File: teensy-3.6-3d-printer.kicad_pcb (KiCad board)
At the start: 2 copper layers, 128.3 x 100.3 mm, 89 parts, among them J1 X_STEPPER, J10 AUX_STEPPER, J11 X-Min-Limit, J12 X-Max-Limit, J13 Y-Min-Limit, J14 Y-Max-Limit, J15 Z-Min-Limit, J16 Z-Max-Limit, J17 Temp0, J18 Temp1, J19 Bed-Temp, J2 Y_STEPPER, J20 3.3V, J21 5V, J22 Conn_02x20_Counter_Clockwise, J23 GND, J25 teensy_back_pins, J26 Extruder 0 Fan, J27 Extruder 0 Part Fan, J28 Aux Fan, J29 12V, J3 Z_STEPPER, J30 12V, J31 Debug, J32 Printer Power IN, J33 Heated Bed, J34 Hot End 1, J35 Hot End 0, J36 12V, J37 Aux 2 Fan, J4 E0_STEPPER, J5 AUX_STEPPER, J6 X_STEPPER, J7 Y_STEPPER, J8 Z_STEPPER, J9 E0_STEPPER, Q1 PN2222A, Q2 PN2222A, Q3 PN2222A, Q4 PN2222A, Q5 IRLZ44N, Q6 PN2222A, Q7 IRLZ44N, U1 Zonestar-LCD2004, U2 Teensy3.6, U3 L7805

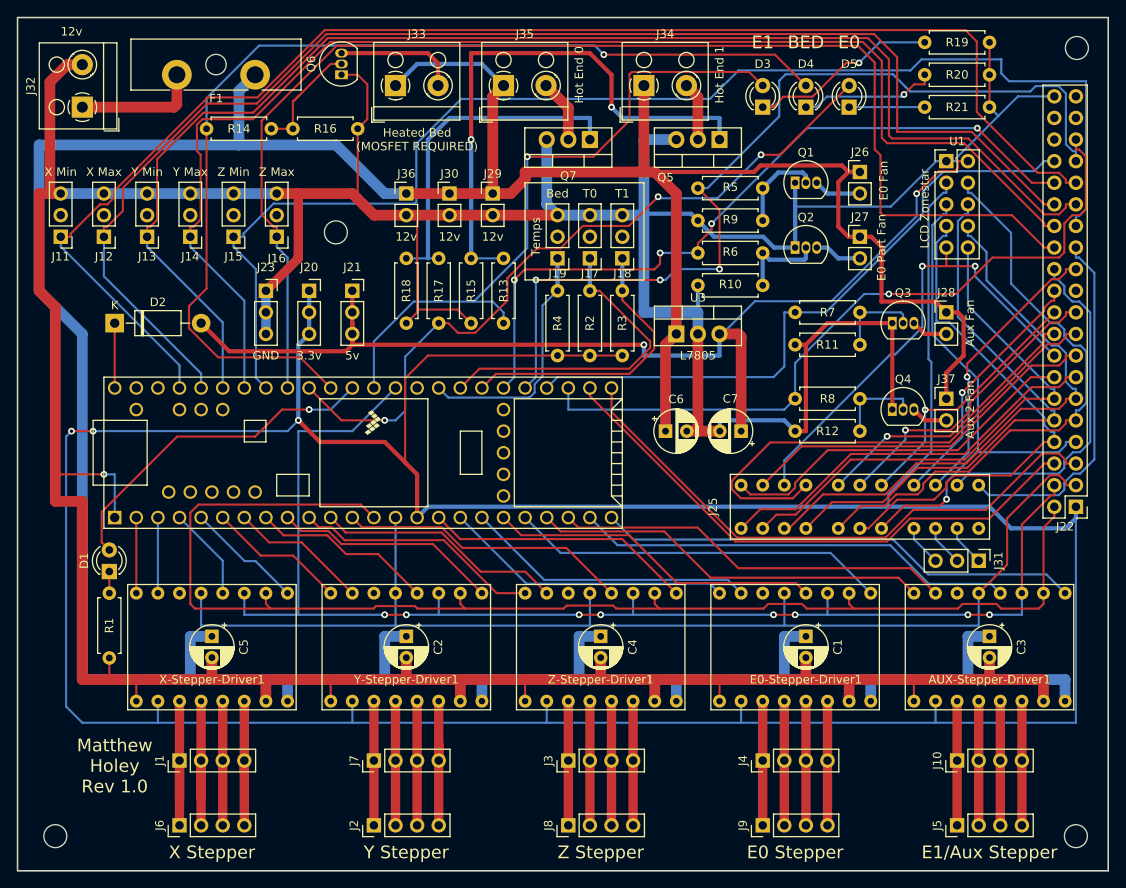
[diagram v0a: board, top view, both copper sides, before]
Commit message: Changed to new fuse holder, added filled zones
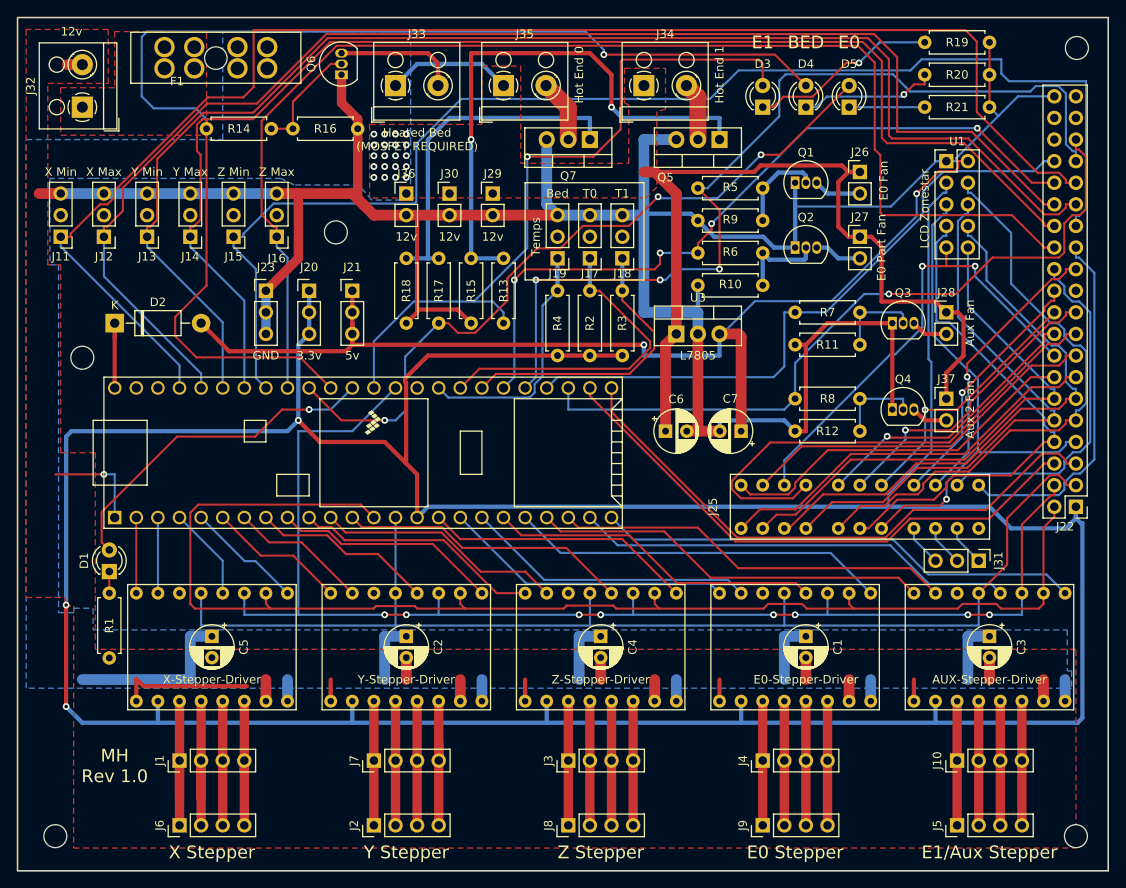
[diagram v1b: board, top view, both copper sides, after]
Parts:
- added REF**: MountingHole_2.7mm_M2.5, MountingHole:MountingHole_2.7mm_M2.5, F.Cu at (101.6, 56.1)
- F1: footprint Fuse:Fuseholder_Blade_ATO_Littelfuse_Pudenz_2_Pin -> fuse:Pudenz-30a-PCB-ATO-Fuseholder
- J20, J21, J23: footprint Connector_PinSocket_2.54mm:PinSocket_1x03_P2.54mm_Vertical -> Connector_PinHeader_2.54mm:PinHeader_1x03_P2.54mm_Vertical
- moved F1 5.03 mm to (117.3, 20.9)
- renumbered AUX-Stepper-Driver1 to AUX-Stepper-Driver, E0-Stepper-Driver1 to E0-Stepper-Driver, X-Stepper-Driver1 to X-Stepper-Driver, Y-Stepper-Driver1 to Y-Stepper-Driver, Z-Stepper-Driver1 to Z-Stepper-Driver
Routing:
- net +12V: track 455.8 -> 177.9 mm, vias 0 -> 20
- net GND: track 551.6 -> 381.8 mm
- net +3V3: track 414.0 -> 440.6 mm
- net HEATER_BED: track 122.5 -> 144.9 mm
- net Net-(F1-Pad2): track 14.7 -> 0.00 mm
- net HEATER_E1: track 79.7 -> 83.9 mm
- net X_MIN: track 166.2 -> 170.1 mm
- net E0_HEATER_12V: track 7.44 -> 11.2 mm
- added copper zone on B.Cu, net +12V
- added copper zone on F.Cu, net +12V
- added copper zone on F.Cu, net GND
- added copper zone on F.Cu, net Net-(F1-Pad2)
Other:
- board text added: "MH Rev 1.0"
- board text removed: "Matthew Holey Rev 1.0"
